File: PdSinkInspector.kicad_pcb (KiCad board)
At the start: 2 copper layers, 62 x 50 mm, 61 parts, among them IC2 STUSB4700YQTR, J1 USB_C_Receptacle_USB2.0_16P, J2 Conn_01x12_Socket, J3 USB_C_Receptacle_USB2.0_16P, Q1 AO3401A, Q2 AO3401A, Q3 AO3401A, SW1 SW_MEC_5E, SW2 SW_MEC_5E, U1 RP2040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

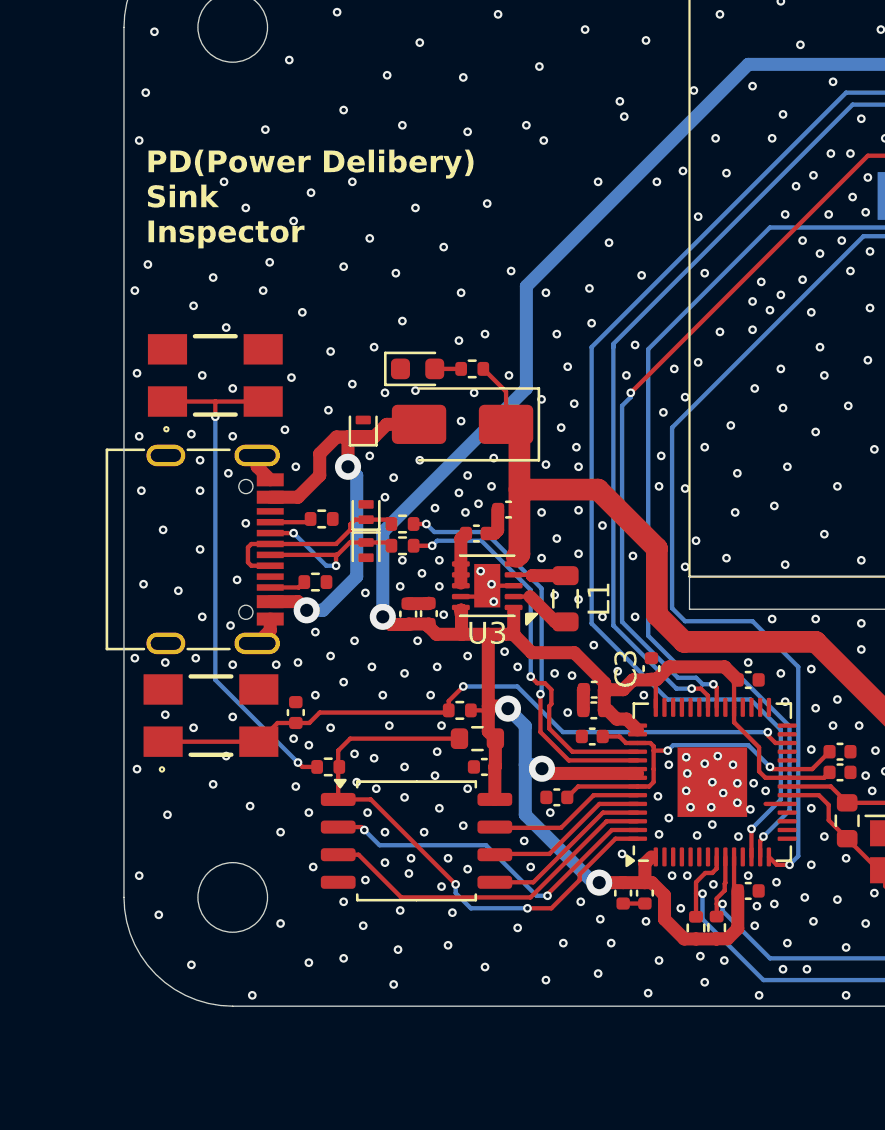
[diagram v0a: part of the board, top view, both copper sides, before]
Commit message: [Update]シルクの印字調整
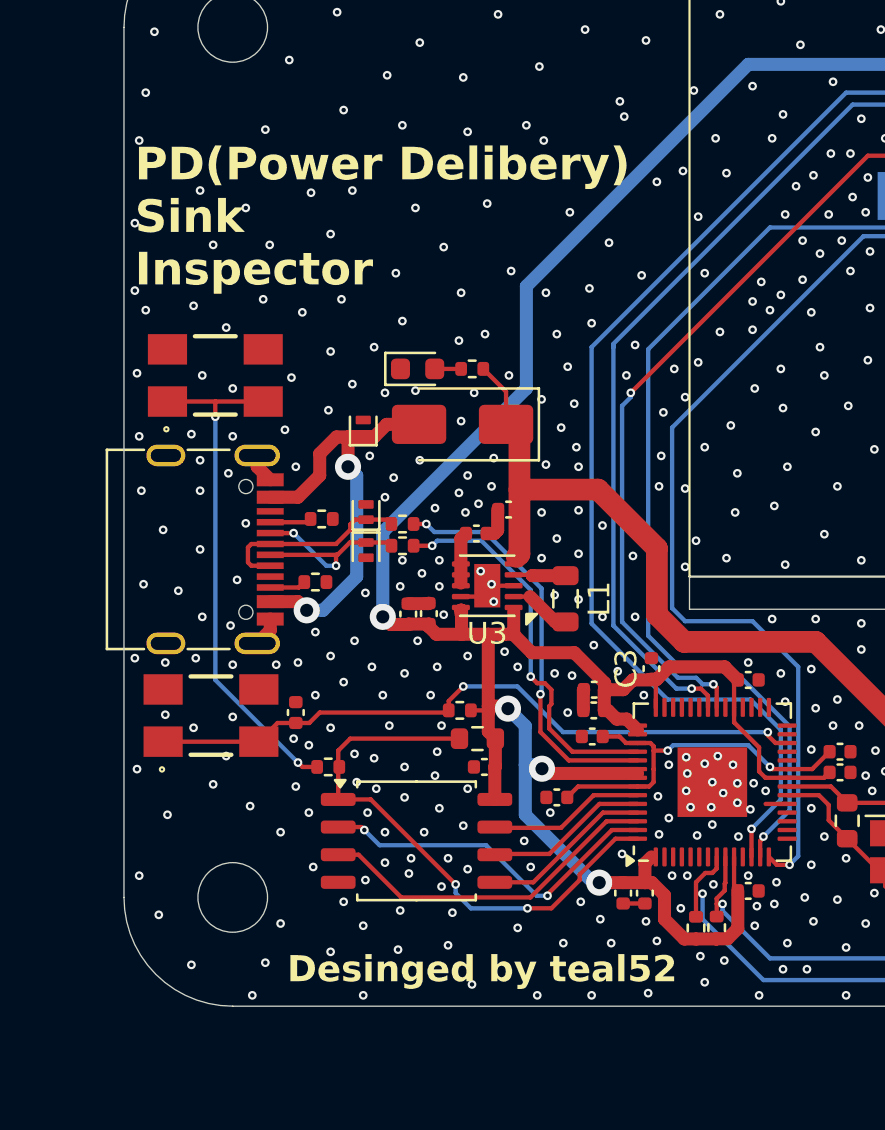
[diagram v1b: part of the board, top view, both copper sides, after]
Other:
- board text added: "Desinged by teal52"
